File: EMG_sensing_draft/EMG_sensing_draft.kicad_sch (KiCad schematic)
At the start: 54 parts, among them J1 EMG_SIGNAL, J2 USB_A_0480370001, J3 DEBUG, U1 W25Q128JV, U2 RN4871-I/RM140, U3 RP2040, U4 OPAMP, U5 MCP1702T-3302E_CB, U6 OPAMP, U7 OPAMP, U8 MCP6N11-002E/SN, U9 OPAMP, Y1 12MHz

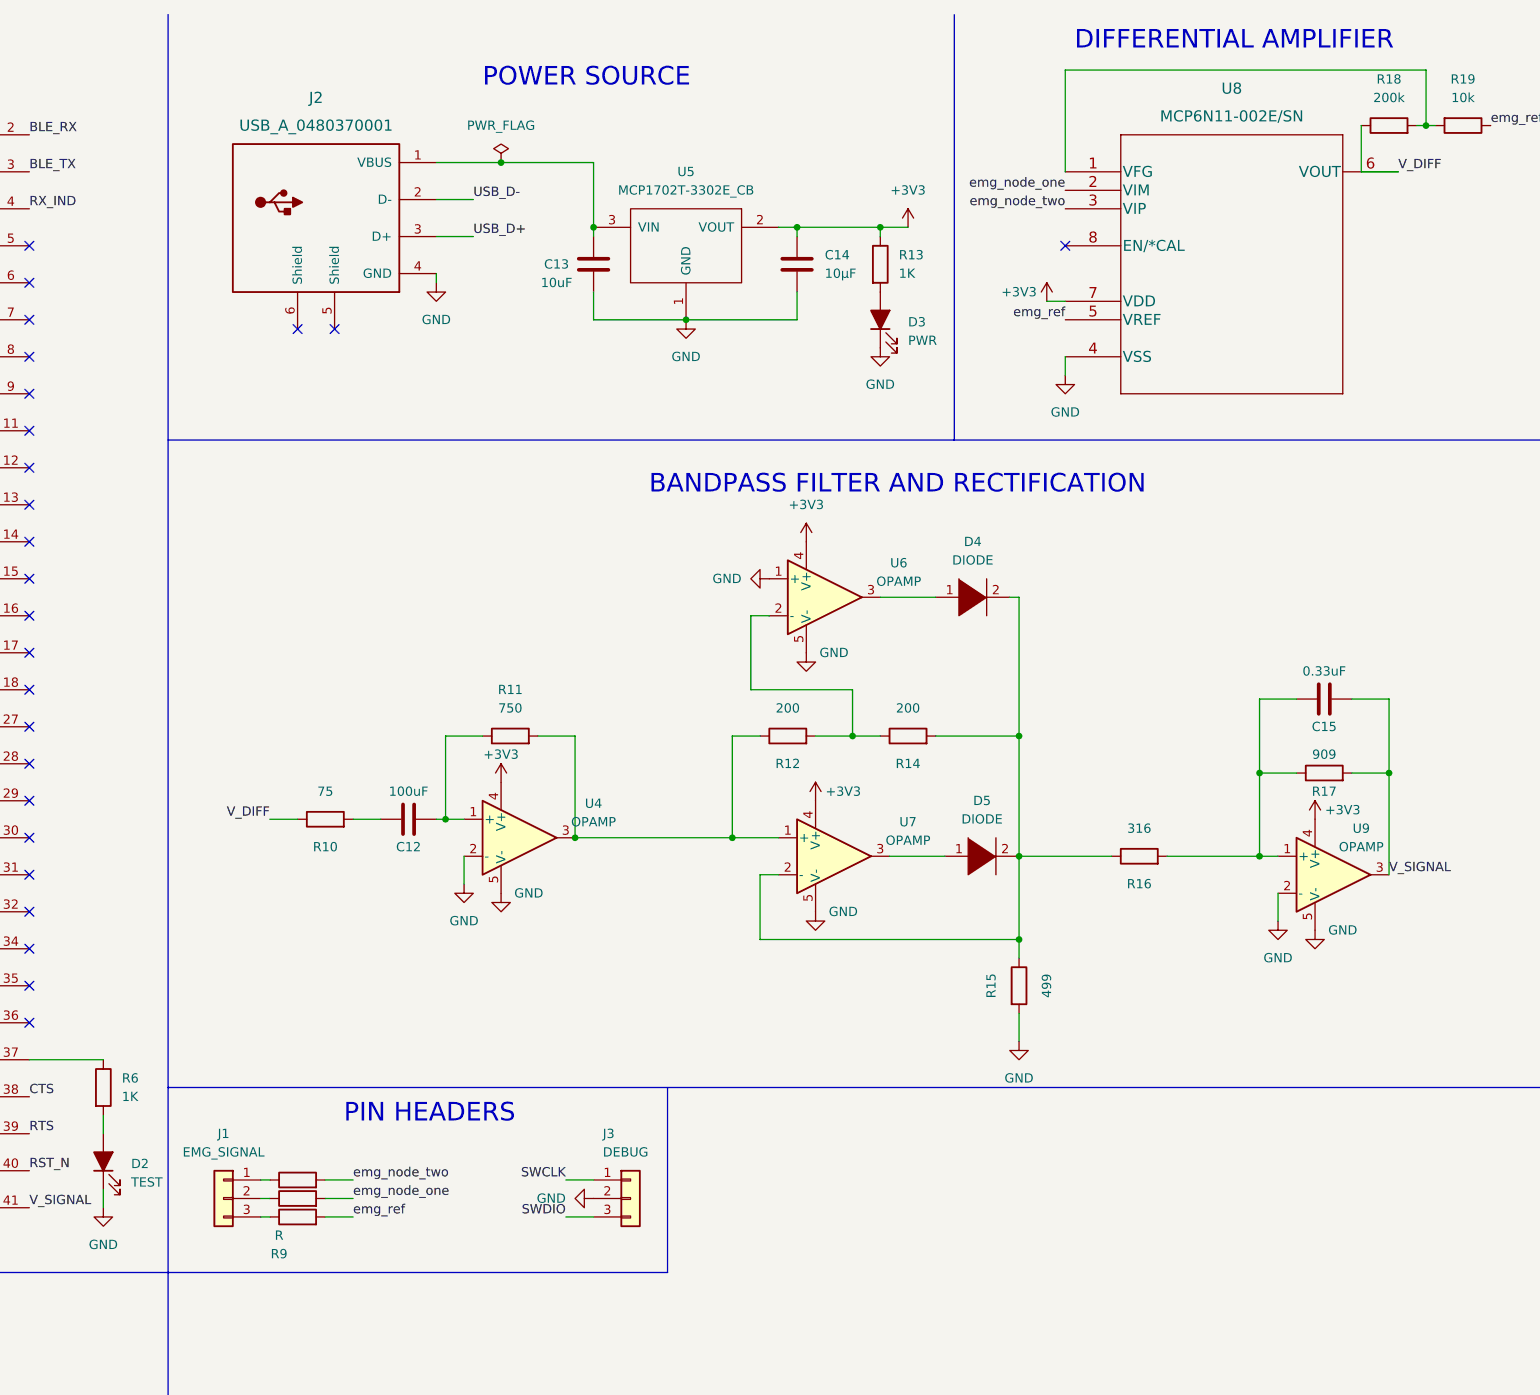
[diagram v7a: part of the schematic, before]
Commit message: Updated resistor values
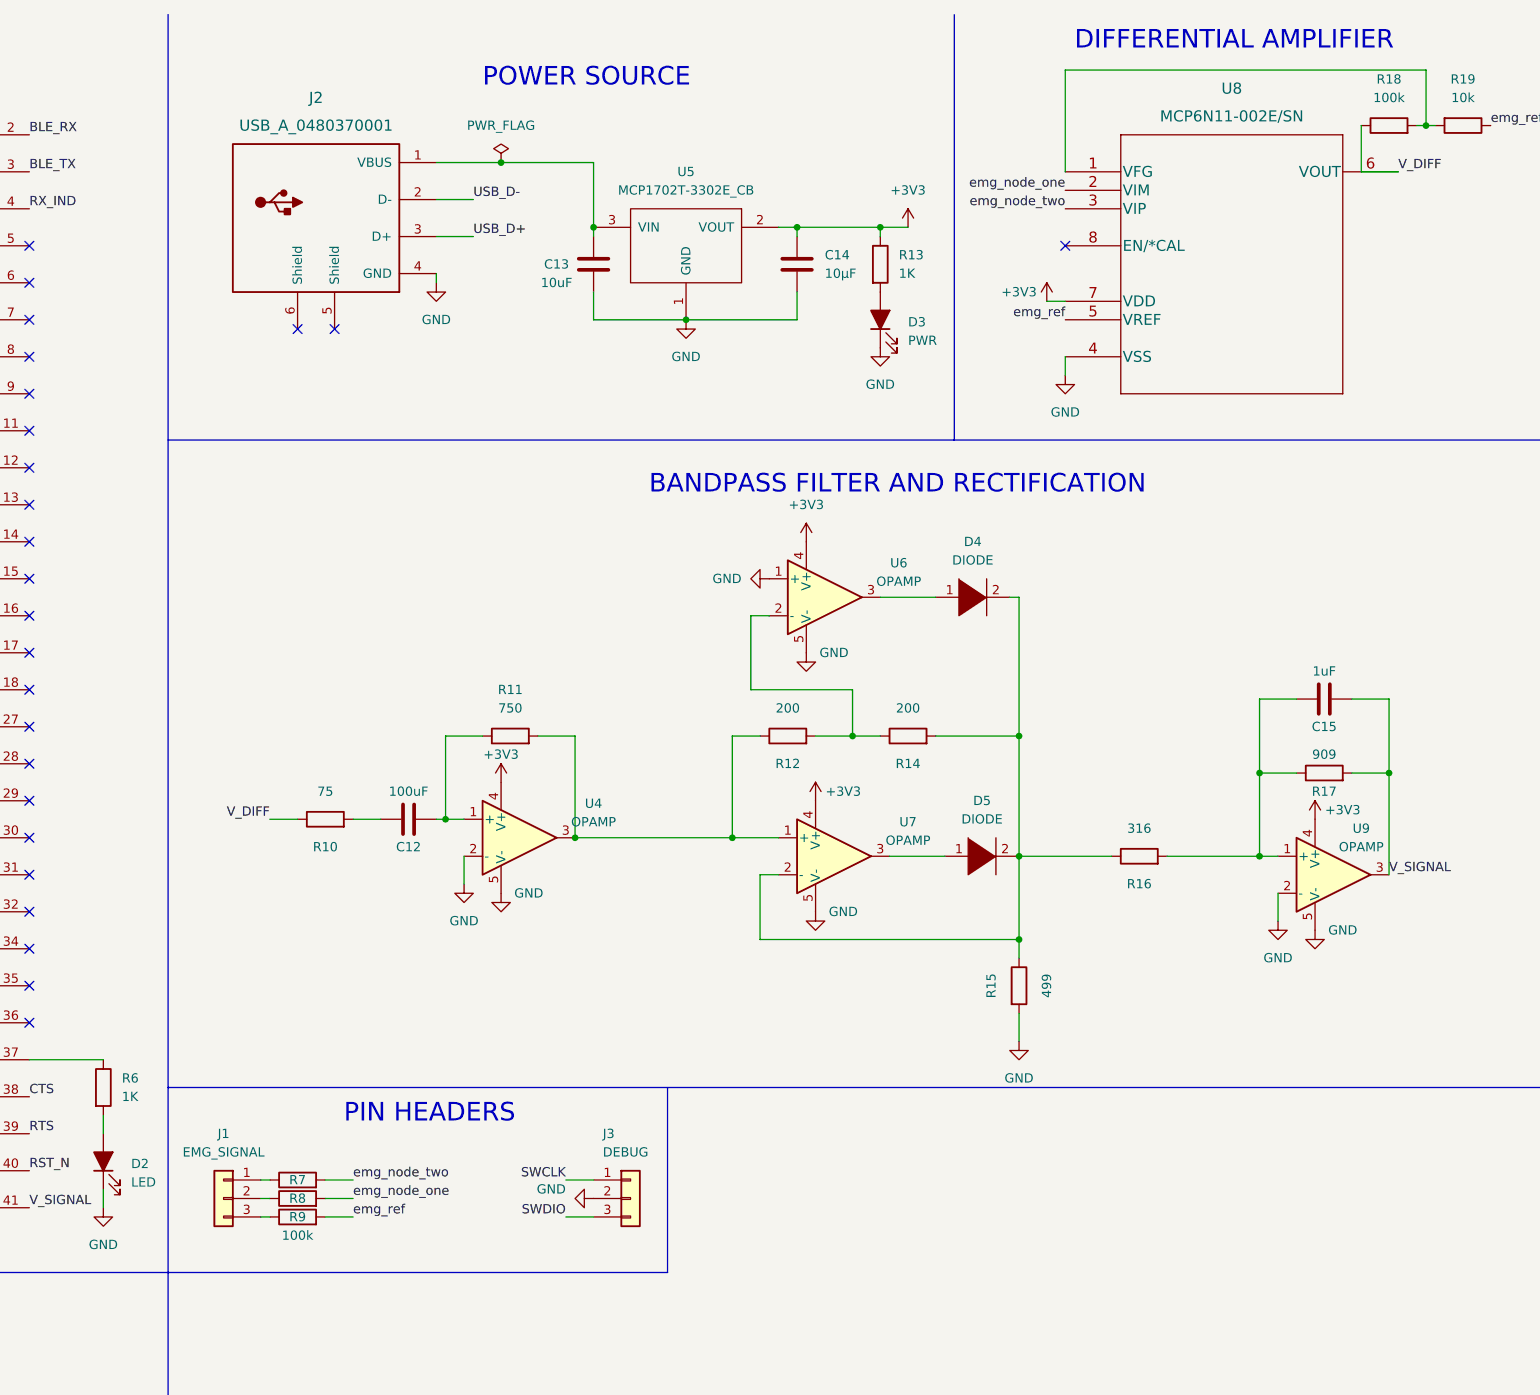
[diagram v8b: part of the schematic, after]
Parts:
- C15: value 0.33uF -> 1uF
- D2: value TEST -> LED
- R18: value 200k -> 100k
- R9: value R -> 100k
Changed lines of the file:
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@@
     (in_bom yes) (on_board yes)
     (property "Reference" "C15" (id 0) (at 314.96 110.49 90))
-    (property "Value" "0.33uF" (id 1) (at 314.96 102.87 90))
+    (property "Value" "1uF" (id 1) (at 314.96 102.87 90))
     (property "Footprint" "" (id 2) (at 318.77 105.7148 0)
       (effects (font (size 1.27 1.27)) hide)
@@
       (effects (font (size 1.27 1.27)) (justify right))
     )
-    (property "Value" "TEST" (id 1) (at 151.13 173.0374 90)
+    (property "Value" "LED" (id 1) (at 151.13 173.0374 90)
       (effects (font (size 1.27 1.27)) (justify right))
     )
@@
   )
   (symbol (lib_id "Device:R") (at 173.99 172.72 90) (unit 1)
-    (in_bom yes) (on_board yes) (fields_autoplaced)
-    (property "Reference" "R7" (id 0) (at 173.99 166.37 90)
-      (effects (font (size 1.27 1.27)) hide)
-    )
+    (in_bom yes) (on_board yes)
+    (property "Reference" "R7" (id 0) (at 173.99 172.72 90))
     (property "Value" "R" (id 1) (at 173.99 168.91 90)
       (effects (font (size 1.27 1.27)) hide)
@@
   )
   (symbol (lib_id "power:GND") (at 214.63 175.26 270) (unit 1)
-    (in_bom yes) (on_board yes) (fields_autoplaced)
+    (in_bom yes) (on_board yes)
     (property "Reference" "#PWR023" (id 0) (at 208.28 175.26 0)
       (effects (font (size 1.27 1.27)) hide)
     )
-    (property "Value" "GND" (id 1) (at 210.82 175.2599 90)
+    (property "Value" "GND" (id 1) (at 210.82 173.99 90)
       (effects (font (size 1.27 1.27)) (justify right))
     )
@@
   (symbol (lib_id "Device:R") (at 173.99 177.8 90) (unit 1)
     (in_bom yes) (on_board yes)
-    (property "Reference" "R9" (id 0) (at 171.45 182.88 90))
-    (property "Value" "R" (id 1) (at 171.45 180.34 90))
+    (property "Reference" "R9" (id 0) (at 173.99 177.8 90))
+    (property "Value" "100k" (id 1) (at 173.99 180.34 90))
     (property "Footprint" "" (id 2) (at 173.99 179.578 90)
       (effects (font (size 1.27 1.27)) hide)
@@
   )
   (symbol (lib_id "Device:R") (at 173.99 175.26 90) (unit 1)
-    (in_bom yes) (on_board yes) (fields_autoplaced)
-    (property "Reference" "R8" (id 0) (at 173.99 168.91 90)
-      (effects (font (size 1.27 1.27)) hide)
-    )
+    (in_bom yes) (on_board yes)
+    (property "Reference" "R8" (id 0) (at 173.99 175.26 90))
     (property "Value" "R" (id 1) (at 173.99 171.45 90)
       (effects (font (size 1.27 1.27)) hide)
@@
     (in_bom yes) (on_board yes) (fields_autoplaced)
     (property "Reference" "R18" (id 0) (at 323.85 21.59 90))
-    (property "Value" "200k" (id 1) (at 323.85 24.13 90))
+    (property "Value" "100k" (id 1) (at 323.85 24.13 90))
     (property "Footprint" "" (id 2) (at 323.85 29.718 90)
       (effects (font (size 1.27 1.27)) hide)
@@
     )
     (path "/0392a271-4134-41ca-8350-e6e1460a370e"
-      (reference "C15") (unit 1) (value "0.33uF") (footprint "")
+      (reference "C15") (unit 1) (value "1uF") (footprint "")
     )
     (path "/edc6d0d1-95cd-4bd8-8476-e09b97bf0890"
@@
     )
     (path "/2a4820de-c377-4e03-8775-f5a166966ff3"
-      (reference "D2") (unit 1) (value "TEST") (footprint "LED_SMD:LED_0805_2012Metric")
+      (reference "D2") (unit 1) (value "LED") (footprint "LED_SMD:LED_0805_2012Metric")
     )
     (path "/b2ef5382-c93c-433d-bae6-7949c1a7f81b"
@@
     )
     (path "/a2add8d8-f471-4447-b22c-c71566a98d5d"
-      (reference "R9") (unit 1) (value "R") (footprint "")
+      (reference "R9") (unit 1) (value "100k") (footprint "")
     )
     (path "/f5f70325-2f2b-4456-91b6-bfaa64c06ac6"
@@
     )
     (path "/fa5c19a9-e166-4278-a194-10b490cea57b"
-      (reference "R18") (unit 1) (value "200k") (footprint "")
+      (reference "R18") (unit 1) (value "100k") (footprint "")
     )
     (path "/da79afc4-af21-4b93-aaed-4ca701f6b222"
